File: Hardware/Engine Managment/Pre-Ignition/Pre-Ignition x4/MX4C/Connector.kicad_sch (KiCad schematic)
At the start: 14 parts, among them J1 Conn_02x12_Counter_Clockwise, J2 Serial0, J3 Serial3, J5 Conn_02x12_Counter_Clockwise, J7 Conn_02x10_Counter_Clockwise

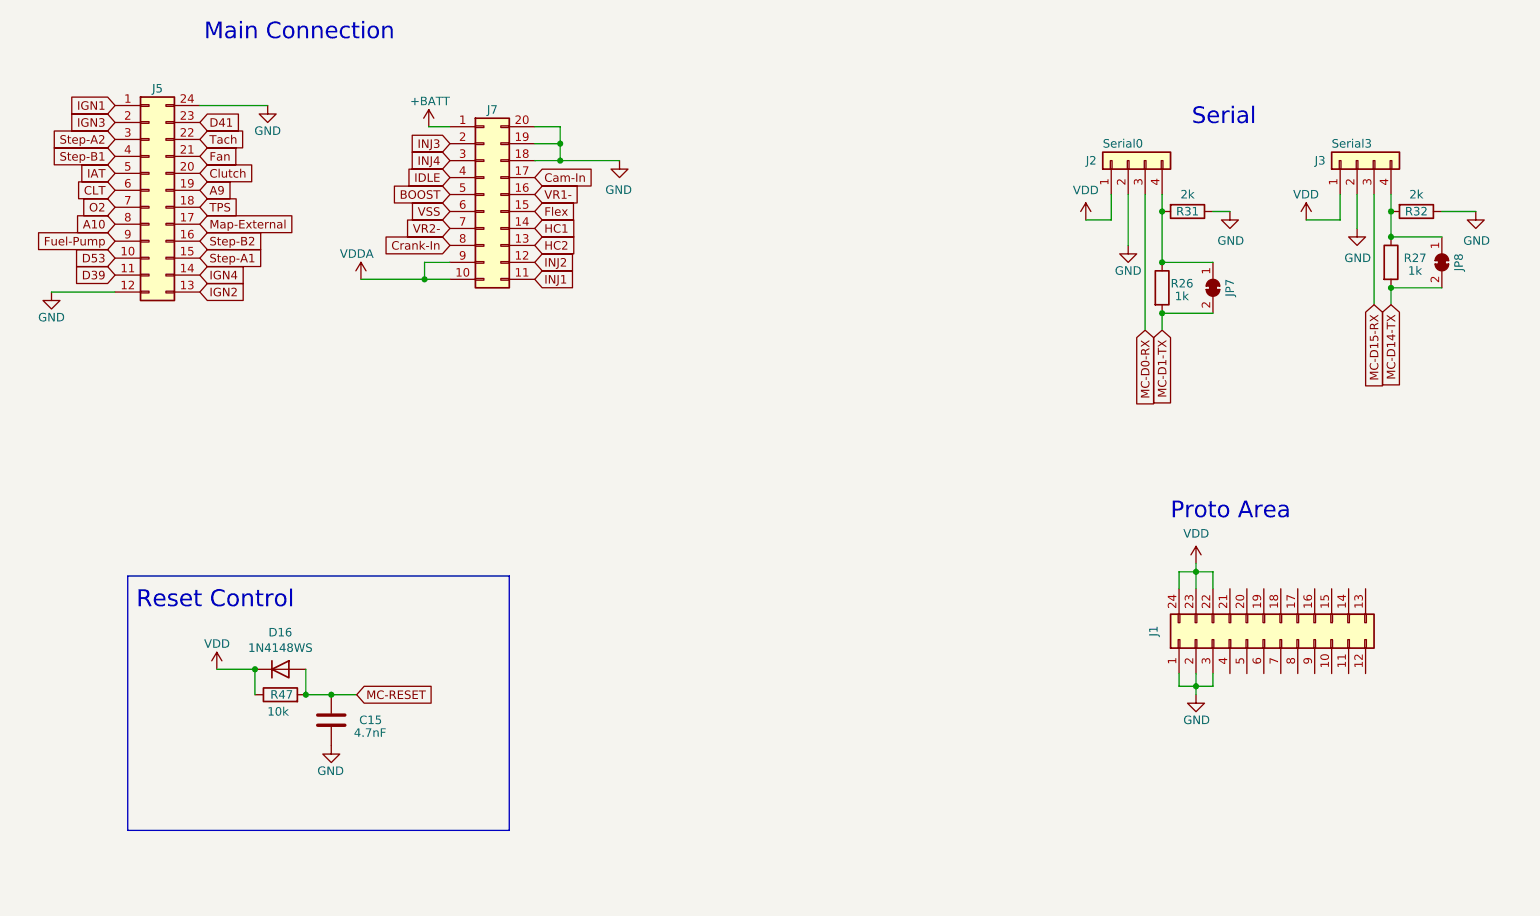
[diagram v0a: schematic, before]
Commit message: Upload correct initial upload files
Initial upload files were accidently taken from an alpha folder. 5v pins on main connector had no voltage. To fix the issue on any manufactured boards remove C8 and C9. Then short the pins of the removed capacitors.
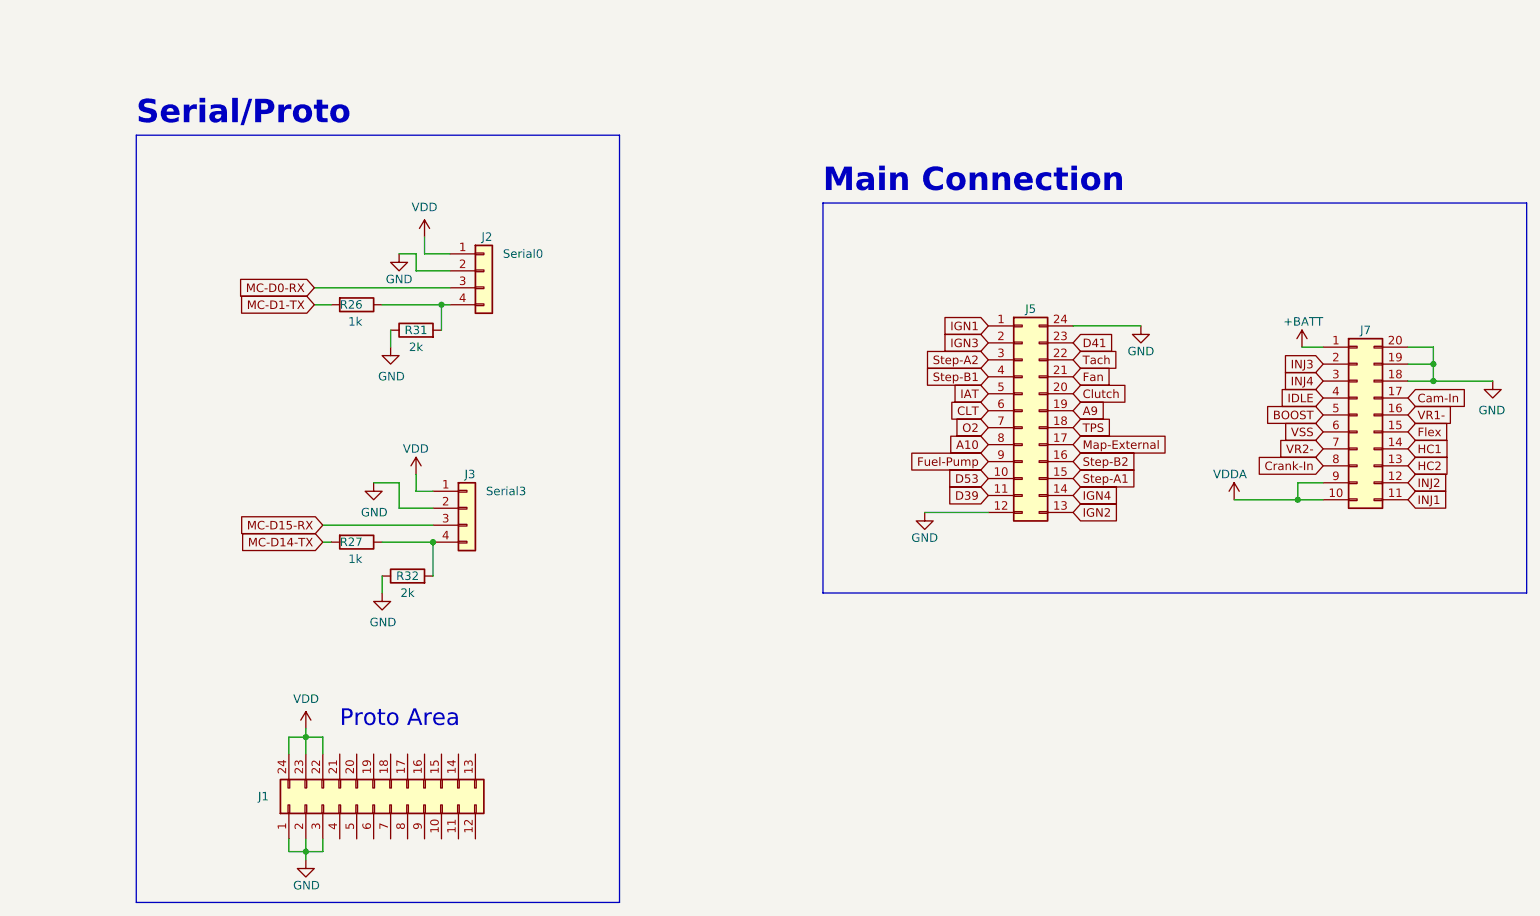
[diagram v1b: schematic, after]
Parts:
- removed C15: 4.7nF, Capacitor_SMD:C_0603_1608Metric, symbol Device:C
- removed D16: 1N4148WS, Diode_SMD:D_SOD-323F, symbol Device:D
- removed JP7, JP8: SolderJumper_2_Bridged, Jumper:SolderJumper-2_P1.3mm_Bridged_RoundedPad1.0x1.5mm, symbol Jumper:SolderJumper_2_Bridged
- removed R47: 10k, Resistor_SMD:R_0603_1608Metric, symbol Device:R
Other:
- note added: "Serial/Proto"
- note removed: "Reset Control"
- note removed: "Serial"
- moved on the sheet: J1, J2, J3, J5, J7, R26, R27, R31, R32

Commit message: Structure Update
MX2 - RevB Upload
MX4B-2 - KiCad Version update (no changes)
MX4C - Organized Schematic, Minor layout change
Engine Simulator 8 Channel - Organized Schematic (no changes)
PMAP-M - Map Sensor Breakout for MX4C
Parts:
- renumbered J2 to J1, J3 to J2, J1 to J3, J7 to J4, J5 to J6
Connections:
- net VDDA is gone; now on net +5V: J4.10 (Pin_10), J4.9 (Pin_9)
- net VDD renamed +5V
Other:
- moved on the sheet: J1, J2, J3, J4, J6, R26, R27, R31, R32

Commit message: minor update
Copper Pour and clearances updated.
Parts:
- renumbered R32 to R19, R27 to R20, R26 to R29, R31 to R33
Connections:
- net HC1 renamed IDLE2
- net HC2 renamed VVT
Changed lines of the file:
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@@
   (title_block
     (title "Pre-Ignition X4")
-    (date "2023-06-15")
+    (date "2023-10-24")
     (rev "C")
     (company "DetonationEMS")
@@
     )
   )
+  (global_label "IDLE2" (shape input) (at 134.62 93.98 0) (fields_autoplaced)
+    (effects (font (size 1.27 1.27)) (justify left))
+    (property "Intersheetrefs" "${INTERSHEET_REFS}" (at 142.2124 93.98 0)
+      (effects (font (size 1.27 1.27)) (justify left) hide)
+    )
+  )
   (global_label "Fuel-Pump" (shape input) (at 71.755 95.885 180) (fields_autoplaced)
     (effects (font (size 1.27 1.27)) (justify right))
@@
     )
   )
-  (global_label "HC2" (shape input) (at 134.62 96.52 0) (fields_autoplaced)
-    (effects (font (size 1.27 1.27)) (justify left))
-    (property "Intersheetrefs" "${INTERSHEET_REFS}" (at 27.94 148.59 0)
-      (effects (font (size 1.27 1.27)) (justify right) hide)
+  (global_label "VVT" (shape input) (at 134.62 96.52 0) (fields_autoplaced)
+    (effects (font (size 1.27 1.27)) (justify left))
+    (property "Intersheetrefs" "${INTERSHEET_REFS}" (at 140.0958 96.52 0)
+      (effects (font (size 1.27 1.27)) (justify left) hide)
     )
   )
@@
     (property "Intersheetrefs" "${INTERSHEET_REFS}" (at 18.415 149.225 0)
       (effects (font (size 1.27 1.27)) (justify left) hide)
-    )
-  )
-  (global_label "HC1" (shape input) (at 134.62 93.98 0) (fields_autoplaced)
-    (effects (font (size 1.27 1.27)) (justify left))
-    (property "Intersheetrefs" "${INTERSHEET_REFS}" (at 27.94 148.59 0)
-      (effects (font (size 1.27 1.27)) (justify right) hide)
     )
   )
@@
   (symbol (lib_id "Device:R") (at 208.28 100.33 90) (unit 1)
     (in_bom yes) (on_board yes) (dnp no)
-    (property "Reference" "R32" (at 208.28 100.33 90)
+    (property "Reference" "R19" (at 208.28 100.33 90)
       (effects (font (size 1.27 1.27)))
     )
@@
       (project "Pre_Ignition"
         (path "/929a9b03-e99e-4b88-8e16-759f8c6b59a5/00000000-0000-0000-0000-000060bdae25"
-          (reference "R32") (unit 1)
+          (reference "R19") (unit 1)
         )
       )
@@
   (symbol (lib_id "Device:R") (at 200.66 59.69 270) (unit 1)
     (in_bom yes) (on_board yes) (dnp no)
-    (property "Reference" "R26" (at 198.12 59.69 90)
+    (property "Reference" "R29" (at 198.12 59.69 90)
       (effects (font (size 1.27 1.27)) (justify left))
     )
@@
       (project "Pre_Ignition"
         (path "/929a9b03-e99e-4b88-8e16-759f8c6b59a5/00000000-0000-0000-0000-000060bdae25"
-          (reference "R26") (unit 1)
+          (reference "R29") (unit 1)
         )
       )
@@
   (symbol (lib_id "Device:R") (at 200.66 95.25 270) (unit 1)
     (in_bom yes) (on_board yes) (dnp no)
-    (property "Reference" "R27" (at 198.12 95.25 90)
+    (property "Reference" "R20" (at 198.12 95.25 90)
       (effects (font (size 1.27 1.27)) (justify left))
     )
@@
       (project "Pre_Ignition"
         (path "/929a9b03-e99e-4b88-8e16-759f8c6b59a5/00000000-0000-0000-0000-000060bdae25"
-          (reference "R27") (unit 1)
+          (reference "R20") (unit 1)
         )
       )
@@
   (symbol (lib_id "Device:R") (at 209.55 63.5 90) (unit 1)
     (in_bom yes) (on_board yes) (dnp no)
-    (property "Reference" "R31" (at 209.55 63.5 90)
+    (property "Reference" "R33" (at 209.55 63.5 90)
       (effects (font (size 1.27 1.27)))
     )
@@
       (project "Pre_Ignition"
         (path "/929a9b03-e99e-4b88-8e16-759f8c6b59a5/00000000-0000-0000-0000-000060bdae25"
-          (reference "R31") (unit 1)
-        )
-      )
+          (reference "R33") (unit 1)
+        )
+      )
